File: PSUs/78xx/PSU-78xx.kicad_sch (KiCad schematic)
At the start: 6 parts

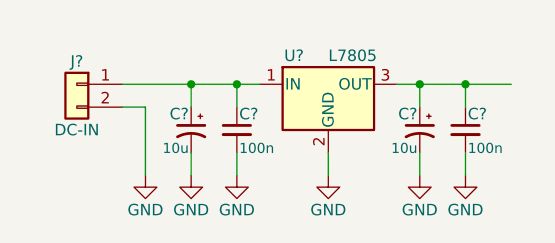
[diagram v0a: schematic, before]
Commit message: Fix grid alignment and update to KiCad 9
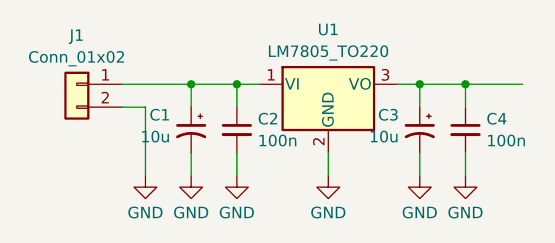
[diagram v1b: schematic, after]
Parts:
- removed C? (x2): 100n, symbol PSU-78xx-rescue:C_Small-PSU-78xx-rescue
- removed C? (x2): 10u, symbol PSU-78xx-rescue:CP1_Small-PSU-78xx-rescue
- removed J?: DC-IN, symbol PSU-78xx-rescue:Conn_01x02-PSU-78xx-rescue
- removed U?: L7805, symbol PSU-78xx-rescue:L7805-PSU-78xx-rescue
- added C1, C3: 10u, symbol Device:C_Polarized_Small_US
- added C2, C4: 100n, symbol Device:C_Small
- added J1: Conn_01x02, symbol Connector_Generic:Conn_01x02
- added U1: LM7805_TO220, Package_TO_SOT_THT:TO-220-3_Vertical, symbol Regulator_Linear:LM7805_TO220
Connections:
- net GND: now also C1.2, C2.2, C3.2, C4.2, J1.2 (Pin_2), U1.2 (GND)
- new net: C1.1, C2.1, J1.1 (Pin_1), U1.1 (VI)
- new net: C3.1, C4.1, U1.3 (VO)
